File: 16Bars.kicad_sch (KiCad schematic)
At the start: 52 parts, among them IC1 CD4033BE, IC2 CD4033BE, IC3 CD4510BE, IC4 CD4510BE, IC5 CD4510BE, J1 3.5mm_Mono_Switched, J2 Conn_02x05_Odd_Even, Q1 2N3904, Q2 2N3904, Q3 2N3904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

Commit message: Revert to through hole resistors.
Get resistor values correct for 16 bars reset AND gate.
Add diode to Q2 reset button transistor.
Fairly certain based on Falstad experiments JLCPCB placed PNP transistors instead of NPN, behavior of reset button in Falstad with PNP matches behavior observed on Rev2.0 PCB giving high reset signal by default and pulling to low when button pressed.
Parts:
- added D6: 1N5819WS, Diode_SMD:D_SOD-323, symbol Device:D
- Q1, Q2, Q3, Q4, Q5: footprint Package_TO_SOT_SMD:SOT-89-3 -> Package_TO_SOT_THT:TO-92_Inline; LCSC C9634 -> (none); Manufacturer_Part_Number C9634 -> (none)
- R23: value 10K -> 470; LCSC C25744 -> C25792; Manufacturer_Part_Number C25744 -> C25792
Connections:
- net RESET: now also D6.1 (K); no longer Q2.3 (C), R14.1
- new net: D6.2 (A), Q2.3 (C), R14.1
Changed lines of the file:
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@@
     (stroke (width 0) (type default) (color 0 0 0 0))
   )
+  (wire (pts (xy 143.51 127) (xy 146.05 127))
+    (stroke (width 0) (type default) (color 0 0 0 0))
+  )
   (wire (pts (xy 62.23 82.55) (xy 62.23 87.63))
     (stroke (width 0) (type default) (color 0 0 0 0))
@@
     (stroke (width 0) (type default) (color 0 0 0 0))
   )
-  (wire (pts (xy 135.89 127) (xy 146.05 127))
-    (stroke (width 0) (type default) (color 0 0 0 0))
-  )
   (wire (pts (xy 34.29 49.53) (xy 41.91 49.53))
     (stroke (width 0) (type default) (color 0 0 0 0))
@@
       (effects (font (size 1.27 1.27)) (justify left))
     )
-    (property "Footprint" "Package_TO_SOT_SMD:SOT-89-3" (id 2) (at 233.68 135.255 0)
+    (property "Footprint" "Package_TO_SOT_THT:TO-92_Inline" (id 2) (at 233.68 135.255 0)
       (effects (font (size 1.27 1.27) italic) (justify left) hide)
     )
-    (property "Datasheet" "https://datasheet.lcsc.com/lcsc/1809192311_Jiangsu-Changjing-Electronics-Technology-Co---Ltd--C9634_C9634.pdf" (id 3) (at 228.6 133.35 0)
+    (property "Datasheet" "https://www.onsemi.com/pdf/datasheet/2n3903-d.pdf" (id 3) (at 228.6 133.35 0)
       (effects (font (size 1.27 1.27)) (justify left) hide)
     )
-    (property "LCSC" "C9634" (id 4) (at 228.6 133.35 0)
+    (property "LCSC" "" (id 4) (at 228.6 133.35 0)
       (effects (font (size 1.27 1.27)) hide)
     )
-    (property "Manufacturer_Part_Number" "C9634" (id 5) (at 228.6 133.35 0)
+    (property "Manufacturer_Part_Number" "" (id 5) (at 228.6 133.35 0)
       (effects (font (size 1.27 1.27)) hide)
     )
@@
       (effects (font (size 1.27 1.27)) (justify right))
     )
-    (property "Value" "10K" (id 1) (at 162.56 127 90)
+    (property "Value" "470" (id 1) (at 162.56 127 90)
       (effects (font (size 1.27 1.27)) (justify right))
     )
@@
       (effects (font (size 1.27 1.27)) hide)
     )
-    (property "LCSC" "C25744" (id 4) (at 162.56 125.73 90)
+    (property "LCSC" "C25792" (id 4) (at 162.56 125.73 90)
       (effects (font (size 1.27 1.27)) hide)
     )
-    (property "Manufacturer_Part_Number" "C25744" (id 5) (at 162.56 125.73 0)
+    (property "Manufacturer_Part_Number" "C25792" (id 5) (at 162.56 125.73 0)
       (effects (font (size 1.27 1.27)) hide)
     )
@@
       (effects (font (size 1.27 1.27)) (justify left))
     )
-    (property "Footprint" "Package_TO_SOT_SMD:SOT-89-3" (id 2) (at 138.43 133.985 0)
+    (property "Footprint" "Package_TO_SOT_THT:TO-92_Inline" (id 2) (at 138.43 133.985 0)
       (effects (font (size 1.27 1.27) italic) (justify left) hide)
     )
-    (property "Datasheet" "https://datasheet.lcsc.com/lcsc/1809192311_Jiangsu-Changjing-Electronics-Technology-Co---Ltd--C9634_C9634.pdf" (id 3) (at 133.35 132.08 0)
+    (property "Datasheet" "https://www.onsemi.com/pdf/datasheet/2n3903-d.pdf" (id 3) (at 133.35 132.08 0)
       (effects (font (size 1.27 1.27)) (justify left) hide)
     )
-    (property "LCSC" "C9634" (id 4) (at 133.35 132.08 0)
-      (effects (font (size 1.27 1.27)) hide)
-    )
-    (property "Manufacturer_Part_Number" "C9634" (id 5) (at 133.35 132.08 0)
-      (effects (font (size 1.27 1.27)) hide)
-    )
     (pin "1")
     (pin "2")
@@
       (effects (font (size 1.27 1.27)) (justify left))
     )
-    (property "Footprint" "Package_TO_SOT_SMD:SOT-89-3" (id 2) (at 165.1 116.205 0)
+    (property "Footprint" "Package_TO_SOT_THT:TO-92_Inline" (id 2) (at 165.1 116.205 0)
       (effects (font (size 1.27 1.27) italic) (justify left) hide)
     )
-    (property "Datasheet" "https://datasheet.lcsc.com/lcsc/1809192311_Jiangsu-Changjing-Electronics-Technology-Co---Ltd--C9634_C9634.pdf" (id 3) (at 160.02 114.3 0)
+    (property "Datasheet" "https://www.onsemi.com/pdf/datasheet/2n3903-d.pdf" (id 3) (at 160.02 114.3 0)
       (effects (font (size 1.27 1.27)) (justify left) hide)
     )
-    (property "LCSC" "C9634" (id 4) (at 160.02 114.3 0)
+    (property "LCSC" "" (id 4) (at 160.02 114.3 0)
       (effects (font (size 1.27 1.27)) hide)
     )
-    (property "Manufacturer_Part_Number" "C9634" (id 5) (at 160.02 114.3 0)
+    (property "Manufacturer_Part_Number" "" (id 5) (at 160.02 114.3 0)
       (effects (font (size 1.27 1.27)) hide)
     )
@@
       (effects (font (size 1.27 1.27)) (justify left))
     )
-    (property "Footprint" "Package_TO_SOT_SMD:SOT-89-3" (id 2) (at 165.1 106.045 0)
+    (property "Footprint" "Package_TO_SOT_THT:TO-92_Inline" (id 2) (at 165.1 106.045 0)
       (effects (font (size 1.27 1.27) italic) (justify left) hide)
     )
-    (property "Datasheet" "https://datasheet.lcsc.com/lcsc/1809192311_Jiangsu-Changjing-Electronics-Technology-Co---Ltd--C9634_C9634.pdf" (id 3) (at 160.02 104.14 0)
+    (property "Datasheet" "https://www.onsemi.com/pdf/datasheet/2n3903-d.pdf" (id 3) (at 160.02 104.14 0)
       (effects (font (size 1.27 1.27)) (justify left) hide)
     )
-    (property "LCSC" "C9634" (id 4) (at 160.02 104.14 0)
+    (property "LCSC" "" (id 4) (at 160.02 104.14 0)
       (effects (font (size 1.27 1.27)) hide)
     )
-    (property "Manufacturer_Part_Number" "C9634" (id 5) (at 160.02 104.14 0)
+    (property "Manufacturer_Part_Number" "" (id 5) (at 160.02 104.14 0)
       (effects (font (size 1.27 1.27)) hide)
     )
@@
       (effects (font (size 1.27 1.27)) (justify left))
     )
-    (property "Footprint" "Package_TO_SOT_SMD:SOT-89-3" (id 2) (at 252.73 130.175 0)
+    (property "Footprint" "Package_TO_SOT_THT:TO-92_Inline" (id 2) (at 252.73 130.175 0)
       (effects (font (size 1.27 1.27) italic) (justify left) hide)
     )
-    (property "Datasheet" "https://datasheet.lcsc.com/lcsc/1809192311_Jiangsu-Changjing-Electronics-Technology-Co---Ltd--C9634_C9634.pdf" (id 3) (at 247.65 128.27 0)
+    (property "Datasheet" "https://www.onsemi.com/pdf/datasheet/2n3903-d.pdf" (id 3) (at 247.65 128.27 0)
       (effects (font (size 1.27 1.27)) (justify left) hide)
     )
-    (property "LCSC" "C9634" (id 4) (at 247.65 128.27 0)
+    (property "LCSC" "" (id 4) (at 247.65 128.27 0)
       (effects (font (size 1.27 1.27)) hide)
     )
-    (property "Manufacturer_Part_Number" "C9634" (id 5) (at 247.65 128.27 0)
+    (property "Manufacturer_Part_Number" "" (id 5) (at 247.65 128.27 0)
       (effects (font (size 1.27 1.27)) hide)
     )
@@
     (pin "1")
   )
+  (symbol (lib_id "Device:D") (at 139.7 127 180) (unit 1)
+    (in_bom yes) (on_board yes)
+    (property "Reference" "D6" (id 0) (at 144.78 120.65 0))
+    (property "Value" "1N5819WS" (id 1) (at 144.78 123.19 0))
+    (property "Footprint" "Diode_SMD:D_SOD-323" (id 2) (at 139.7 127 0)
+      (effects (font (size 1.27 1.27)) hide)
+    )
+    (property "Datasheet" "https://datasheet.lcsc.com/lcsc/2204281430_Guangdong-Hottech-1N5819WS_C191023.pdf" (id 3) (at 139.7 127 0)
+      (effects (font (size 1.27 1.27)) hide)
+    )
+    (property "LCSC" "C191023" (id 4) (at 139.7 127 0)
+      (effects (font (size 1.27 1.27)) hide)
+    )
+    (property "Manufacturer_Part_Number" "C191023" (id 5) (at 139.7 127 0)
+      (effects (font (size 1.27 1.27)) hide)
+    )
+    (pin "1")
+    (pin "2")
+  )
   (symbol (lib_id "power:GND") (at 57.15 199.39 90) (unit 1)
     (in_bom yes) (on_board yes)
@@
       (reference "D5") (unit 1) (value "1N5819WS") (footprint "Diode_SMD:D_SOD-323")
     )
+    (path "/fa48d87f-a604-4797-86af-9aa488121980"
+      (reference "D6") (unit 1) (value "1N5819WS") (footprint "Diode_SMD:D_SOD-323")
+    )
     (path "/273f01f0-28d2-4494-b80f-412095039d4d"
       (reference "DS-ONES1") (unit 1) (value "TDSR0760") (footprint "TDSR*:TDSR0760")
@@
     )
     (path "/10a385da-41ee-4d58-8512-ba1f8981e8db"
-      (reference "Q1") (unit 1) (value "2N3904") (footprint "Package_TO_SOT_SMD:SOT-89-3")
+      (reference "Q1") (unit 1) (value "2N3904") (footprint "Package_TO_SOT_THT:TO-92_Inline")
     )
     (path "/6b9564a2-10d4-43b3-a466-7ed78caf8bbd"
-      (reference "Q2") (unit 1) (value "2N3904") (footprint "Package_TO_SOT_SMD:SOT-89-3")
+      (reference "Q2") (unit 1) (value "2N3904") (footprint "Package_TO_SOT_THT:TO-92_Inline")
     )
     (path "/c1378853-dfc4-4dcf-802c-5be1596f8f74"
-      (reference "Q3") (unit 1) (value "2N3904") (footprint "Package_TO_SOT_SMD:SOT-89-3")
+      (reference "Q3") (unit 1) (value "2N3904") (footprint "Package_TO_SOT_THT:TO-92_Inline")
     )
     (path "/94c0d5e2-1db0-4639-8fdc-be7c8290075c"
-      (reference "Q4") (unit 1) (value "2N3904") (footprint "Package_TO_SOT_SMD:SOT-89-3")
+      (reference "Q4") (unit 1) (value "2N3904") (footprint "Package_TO_SOT_THT:TO-92_Inline")
     )
     (path "/8264cfbb-7c08-4cf8-92b7-6b80ec6ff369"
-      (reference "Q5") (unit 1) (value "2N3904") (footprint "Package_TO_SOT_SMD:SOT-89-3")
+      (reference "Q5") (unit 1) (value "2N3904") (footprint "Package_TO_SOT_THT:TO-92_Inline")
     )
     (path "/3edd593e-f294-4804-b929-bdd933a6f36b"
@@
     )
     (path "/50082213-59b8-4178-ae4c-b6bf80352015"
-      (reference "R23") (unit 1) (value "10K") (footprint "Resistor_SMD:R_0402_1005Metric")
+      (reference "R23") (unit 1) (value "470") (footprint "Resistor_SMD:R_0402_1005Metric")
     )
     (path "/8b86c1c9-cfb9-49b2-bb41-9ca31170ff9d"

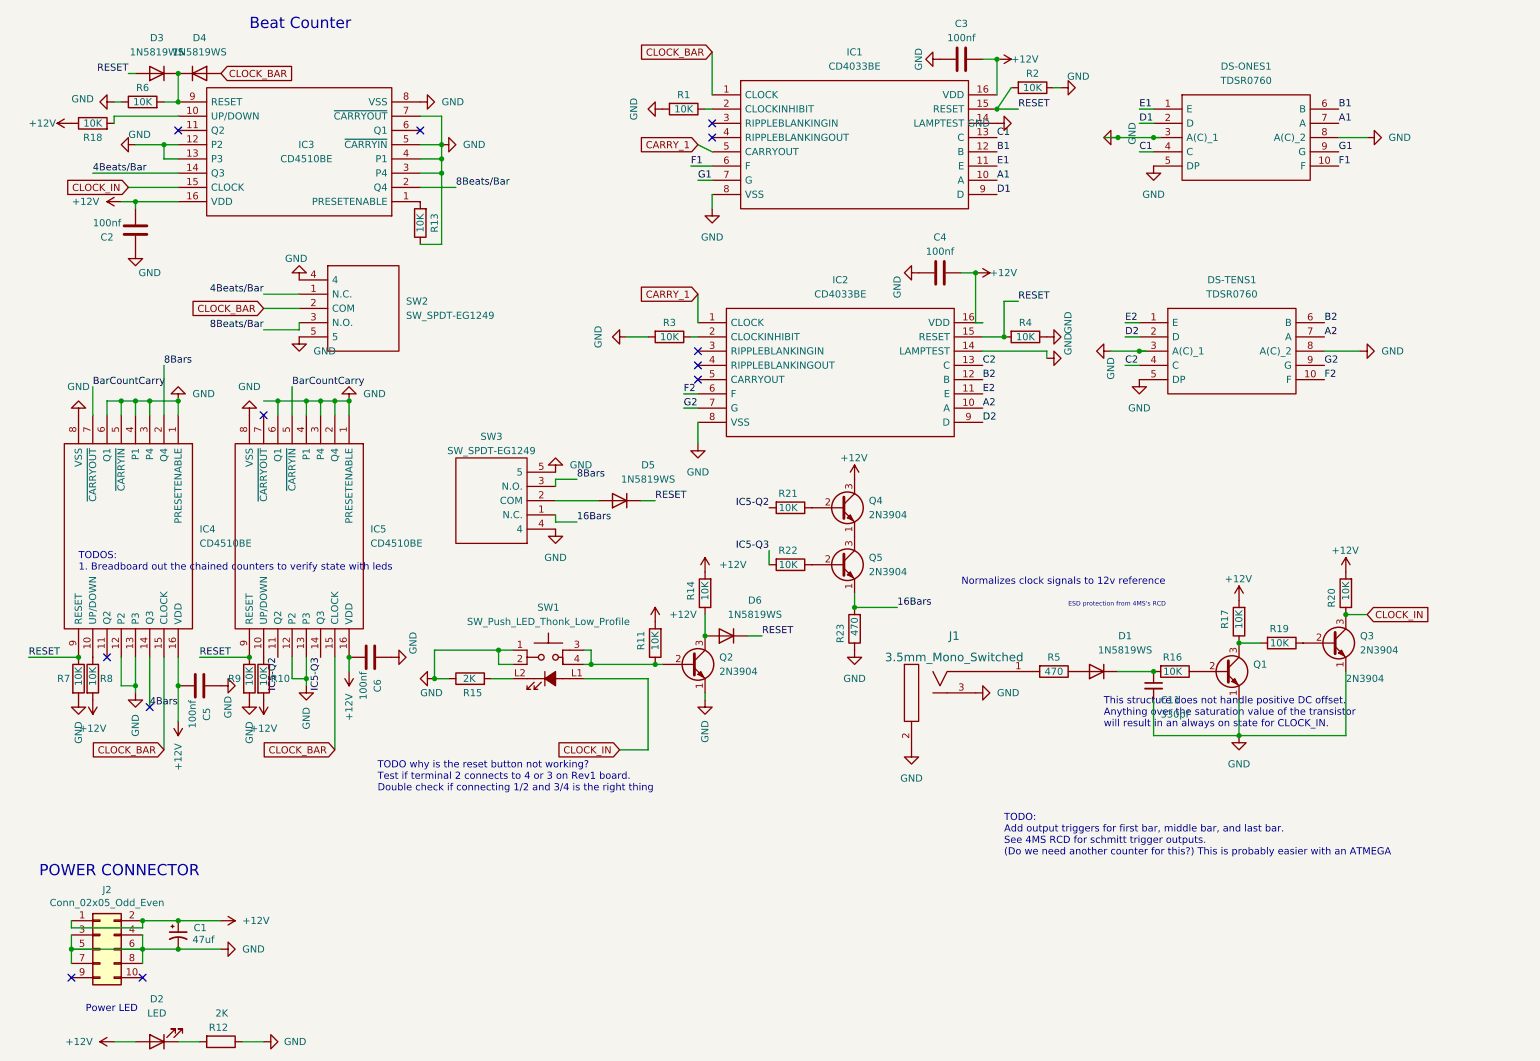
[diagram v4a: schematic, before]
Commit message: Attempt to fix reset logic
Falstad model helped get resistor values dialed in so we're sending >9v when 16 count is reached between the two 4510 counters and 12v is sent from the reset button. Removed diodes to increase voltage as they were adding resistance.
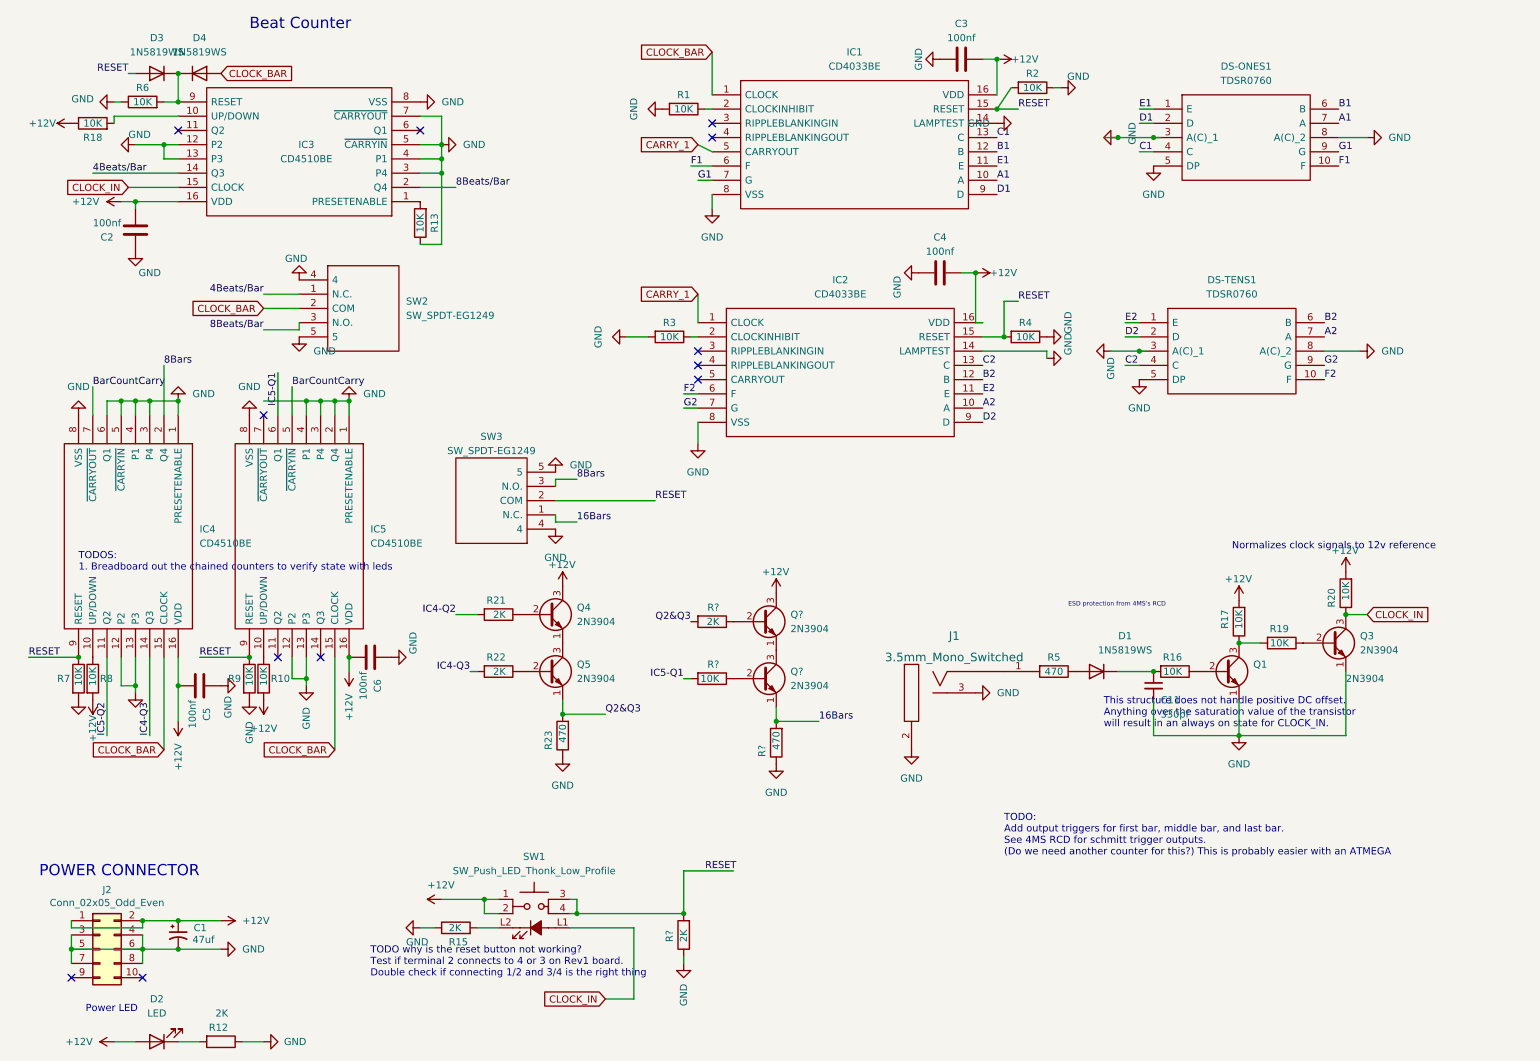
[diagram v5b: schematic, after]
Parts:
- removed D5, D6: 1N5819WS, Diode_SMD:D_SOD-323, symbol Device:D
- removed Q2: 2N3904, Package_TO_SOT_THT:TO-92_Inline, symbol Transistor_BJT:2N3904
- removed R11, R14: 10K, Resistor_SMD:R_0402_1005Metric, symbol Device:R
- added Q? (x2): 2N3904, Package_TO_SOT_THT:TO-92_Inline, symbol Transistor_BJT:2N3904
- added R? (x2): 2K, Resistor_SMD:R_0402_1005Metric, symbol Device:R
- added R?: 470, Resistor_SMD:R_0402_1005Metric, symbol Device:R
- added R?: 10K, Resistor_SMD:R_0402_1005Metric, symbol Device:R
- R21, R22: value 10K -> 2K
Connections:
- net +12V: now also SW1.1, SW1.2, Q?.3 (C)
- net 16Bars: now also Q?.1 (E), R?.2; no longer Q5.1 (E), R23.2
- net GND: now also R?.1, R?.1; no longer IC5.6 (Q1), SW1.1, SW1.2
- net IC5-Q2: now also IC4.11 (Q2); no longer IC5.11 (Q2), R21.2
- net RESET: now also SW1.3, SW1.4, SW3.2 (COM), R?.2
- net 4Bars renamed IC4-Q3
- net IC4-Q3: now also R22.2
- net IC5-Q3: no longer names the net of IC5.14 (Q3)
- net IC5-Q3: no longer R22.2
- new net: Q?.1 (E), Q?.3 (C)
- new net: Q?.2 (B), R?.1 (x2)
- new net IC4-Q2: R21.2
- new net IC5-Q1: IC5.6 (Q1), R?.2
- new net Q2&Q3: Q5.1 (E), R23.2, R?.2
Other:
- moved on the sheet: Q4, Q5, R15, R21, R22, R23, SW1
